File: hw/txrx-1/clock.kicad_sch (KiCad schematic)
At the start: 9 parts, among them U4 Si5351A-B-GT, Y1 CX3225SB25000D0FFFCC

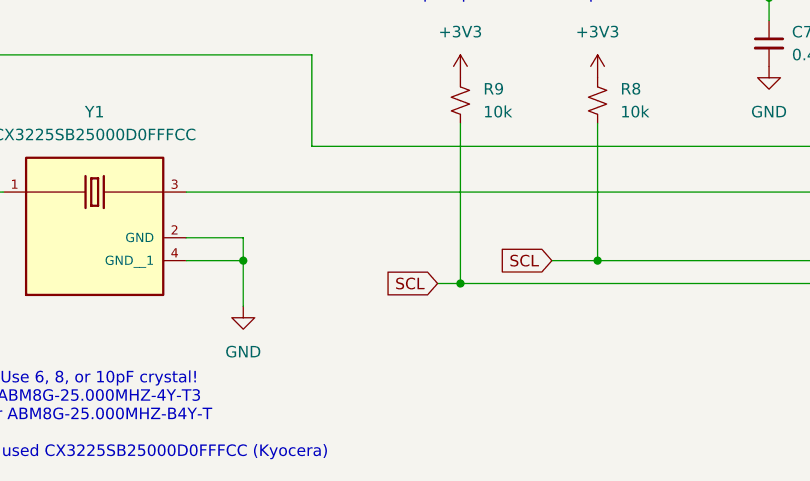
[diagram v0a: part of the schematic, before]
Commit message: Initial PCB layout for TXRX board
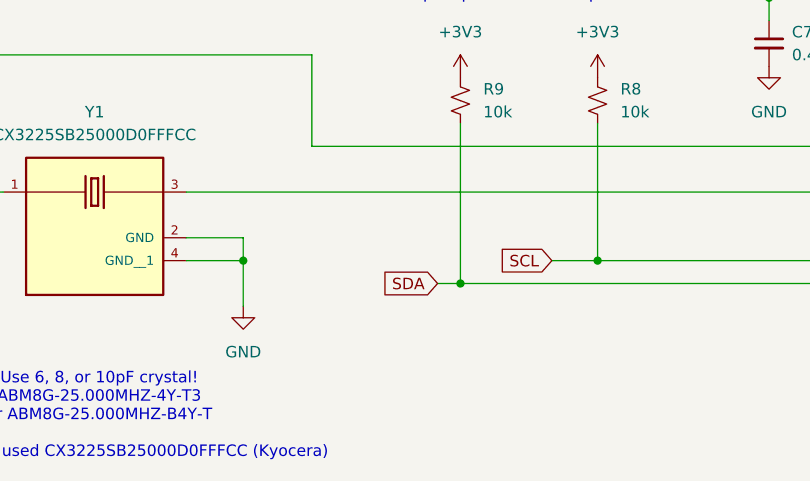
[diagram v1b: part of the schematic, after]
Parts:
- Y1: footprint CX3225SB25000D0FFFCC:OSCCC320X250X60N -> bruce-footprints:OSCCC320X250X60N
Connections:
- net SCL: no longer R9.2, U4.5 (SDA)
- new net SDA: R9.2, U4.5 (SDA)
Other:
- company: (none) -> Bruce MacKinnon KC1FSZ
- title: (none) -> Quadrature TX/RX Board
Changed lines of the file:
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@@
 	(generator "eeschema")
 	(generator_version "8.0")
-	(paper "A4")
+	(paper "USLetter")
+	(title_block
+		(title "Quadrature TX/RX Board")
+		(date "2025-02-16")
+		(rev "1")
+		(company "Bruce MacKinnon KC1FSZ")
+		(comment 1 "Copyright (C) Bruce MacKinnon, 2025")
+		(comment 2 "NOT FOR COMMERCIAL USE")
+	)
 	(junction
 		(at 88.9 97.79)
@@
 		)
 	)
-	(global_label "SCL"
+	(global_label "SDA"
 		(shape input)
 		(at 86.36 97.79 180)
@@
 		)
 		(property "Intersheetrefs" "${INTERSHEET_REFS}"
-			(at 79.8672 97.79 0)
+			(at 79.8067 97.79 0)
 			(effects
 				(font
@@
 			)
 		)
-		(property "Footprint" "CX3225SB25000D0FFFCC:OSCCC320X250X60N"
+		(property "Footprint" "bruce-footprints:OSCCC320X250X60N"
 			(at 48.26 90.17 0)
 			(effects

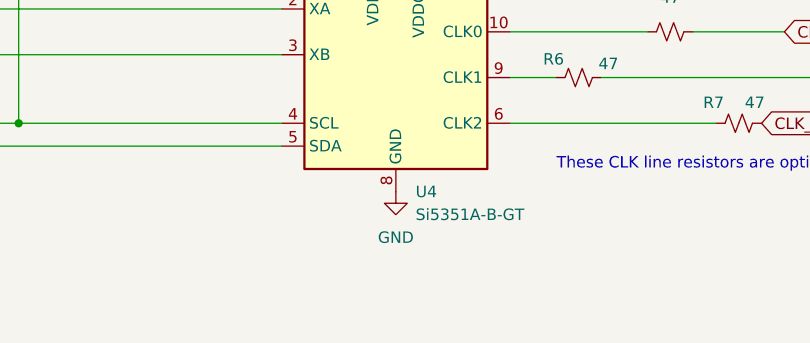
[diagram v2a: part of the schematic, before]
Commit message: Sending revision of util-1 to JLCPCB
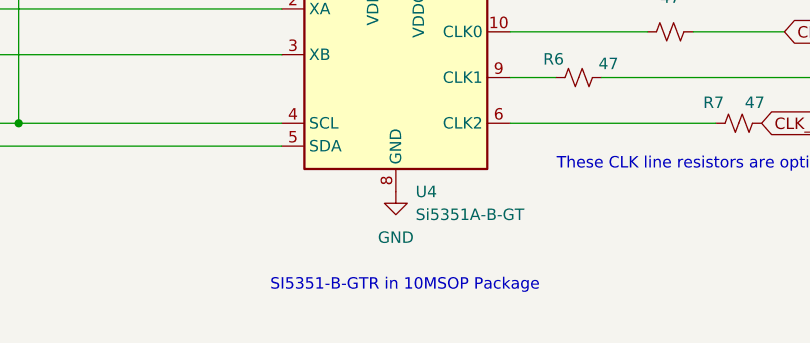
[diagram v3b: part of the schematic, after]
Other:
- note added: "SI5351-B-GTR in 10MSOP Package"
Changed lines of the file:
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@@
+		)
+	)
+	(text "SI5351-B-GTR in 10MSOP Package"
+		(exclude_from_sim no)
+		(at 147.066 113.284 0)
+		(effects
+			(font
+				(size 1.27 1.27)
+			)
 		)
 	)
